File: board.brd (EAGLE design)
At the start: 85 parts, among them J1 AVR_SPI_PRG_6NS, U1 TPS2112A, U2 MAX1555, U3 USD-SOCKETNEW, U4 3.3V, U5 2.8V, U6 74HC595, Y1 8MHz, Y2 12.288MHz

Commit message: 0.1" shrink on y axis
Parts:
- moved JP2 14.9 mm to (41.6, 1.91)
- moved C7 12.8 mm to (64.1, 15.1)
- moved C13 2.54 mm to (21.0, 34.9)
- moved C9 2.54 mm to (19.1, 34.9)
- moved R15 2.54 mm to (41.9, 34.9)
- moved R9 2.54 mm to (38.7, 34.9)
- moved C16 2.54 mm to (23.8, 31.1)
- moved LED3 2.54 mm to (40.3, 16.2)
- moved LED6 2.54 mm to (40.3, 21.9)
- moved R11 2.54 mm to (23.8, 29.5)
- moved R13 2.54 mm to (23.8, 27.6)
- moved R23 2.54 mm to (44.5, 16.2)
- moved R26 2.54 mm to (44.5, 21.9)
- moved R6 2.54 mm to (22.2, 19.7)
- moved U1 2.54 mm to (8.26, 31.1)
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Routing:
- net SERIAL_TX: track 12.0 -> 22.1 mm
- net SERIAL_RX: track 10.7 -> 18.9 mm
- net VDD: track 243.3 -> 241.6 mm, vias 8 -> 9
- net ENCODER_A: track 39.5 -> 40.6 mm
- net ENCODER_B: track 34.5 -> 33.8 mm

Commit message: Moved SPI header to fit battery
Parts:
- moved J1 2.71 mm to (5.40, 5.08)
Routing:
- net VDD: track 241.6 -> 236.6 mm
- net RESET: track 15.4 -> 18.3 mm
- net MOSI: track 88.4 -> 86.2 mm
- net SCK: track 74.3 -> 76.3 mm, vias 2 -> 3
- net MISO: track 84.0 -> 82.1 mm
- net SERIAL_TX: track 22.1 -> 21.3 mm
- net SERIAL_RX: track 18.9 -> 18.3 mm
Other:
- board outline added: 50.8 x 33.5 mm

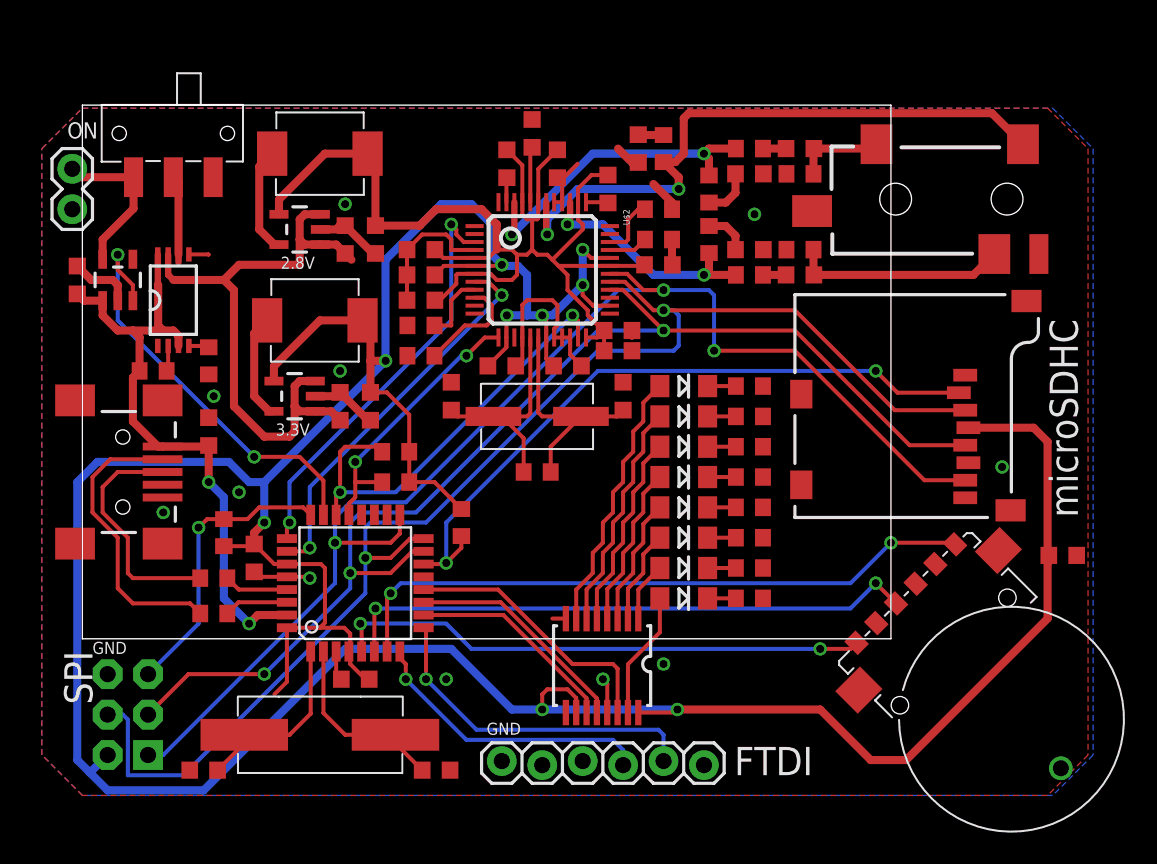
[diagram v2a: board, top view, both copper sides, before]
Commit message: Moved battery plug and SD capacitor
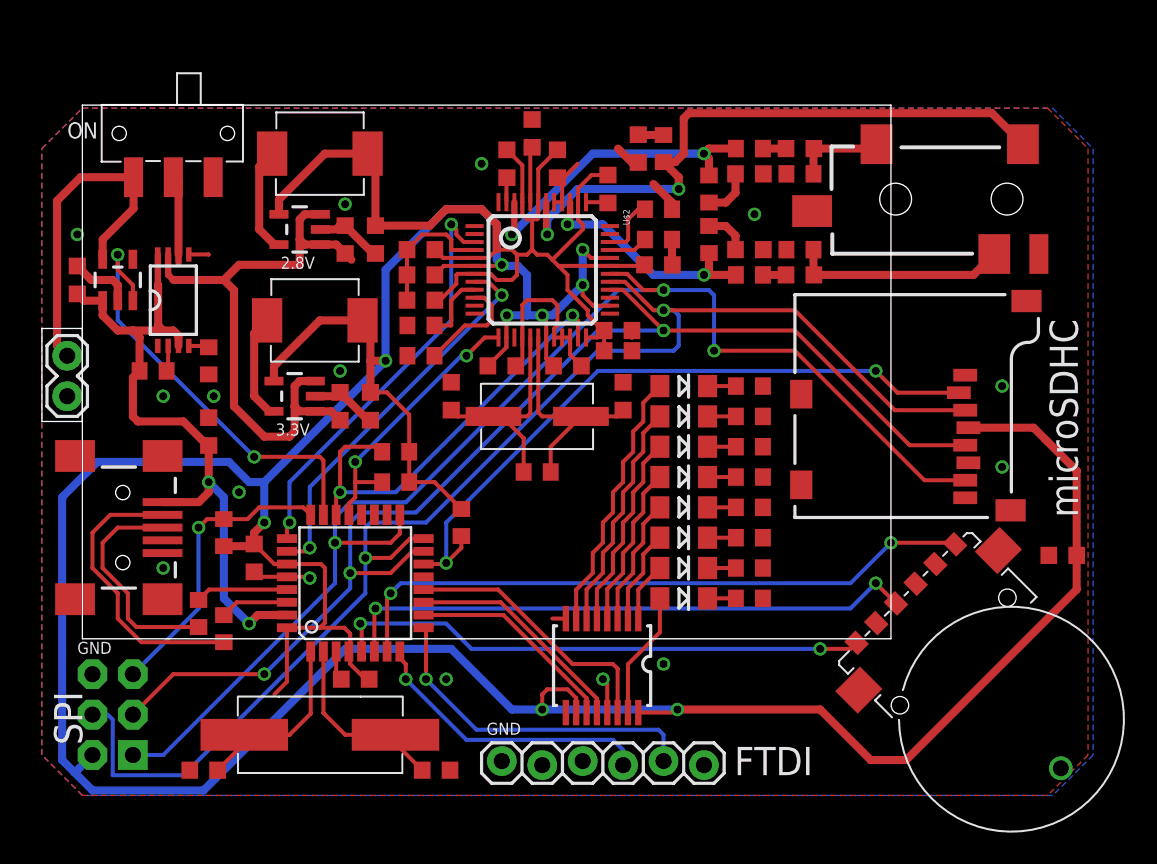
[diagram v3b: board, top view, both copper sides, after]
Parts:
- moved JP3 11.8 mm to (1.59, 27.6)
- moved JP1 3.49 mm to (5.08, 16.8)
- moved R2 2.42 mm to (9.84, 11.4), turned to 270 degrees
- moved R1 1.14 mm to (11.4, 10.5), turned to 270 degrees
- moved J1 0.95 mm to (4.45, 5.08)
- turned C7 to 180 degrees
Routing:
- net VBAT: track 10.0 -> 21.4 mm
- net VBUS: track 39.9 -> 43.5 mm
- net VDD: track 236.6 -> 238.5 mm
- net USB_D+: track 4.04 -> 5.82 mm
- net SCK: track 76.3 -> 77.3 mm
- net MISO: track 82.1 -> 83.1 mm
- net MOSI: track 86.2 -> 87.2 mm
- net CHG_B: track 26.7 -> 27.4 mm
- net N$6: track 14.9 -> 14.3 mm
- net GND: vias 11 -> 15
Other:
- board size 50.8 x 33.5 mm -> 53.3 x 33.5 mm

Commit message: Switched audio plug to 3-pin version and added OE connection
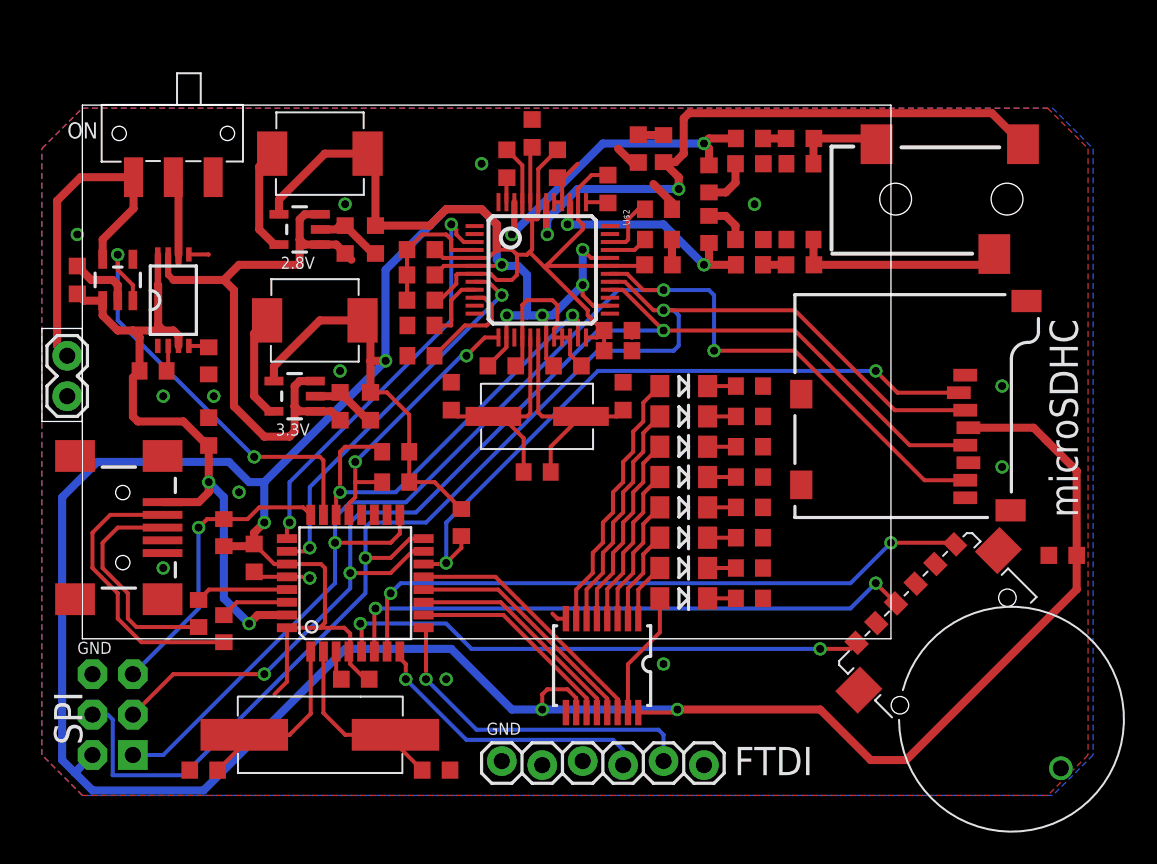
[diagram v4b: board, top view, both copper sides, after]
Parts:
- U7: device SparkFun-Connectors:AUDIO-JACK-3.5MM-SMD -> mkmp3:AUDIO-JACK-3.5MM-SMD
- moved R15 0.64 mm to (41.9, 35.6)
- moved C27 0.63 mm to (44.5, 34.9)
- moved C28 0.63 mm to (44.5, 39.7)
- moved C29 0.63 mm to (47.6, 41.3)
- moved C30 0.63 mm to (47.6, 33.3)
- moved R16 0.63 mm to (41.9, 38.7)
- moved R17 0.63 mm to (44.5, 41.3)
- moved R18 0.63 mm to (44.5, 33.3)
- moved R19 0.63 mm to (47.6, 34.9)
- moved R20 0.63 mm to (47.6, 39.7)
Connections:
- new net SHIFT_OE: U$1.12, U6.13
- net DS: now also U$1.13; no longer U$1.12
- net GND: no longer U6.13
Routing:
- net SHIFT_OE: track 0.00 -> 15.3 mm
- net GND: track 57.0 -> 54.9 mm, vias 15 -> 14
- net CVDD: track 72.3 -> 73.3 mm
- net DS: track 17.0 -> 16.2 mm

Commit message: Fixed rear silkscreen
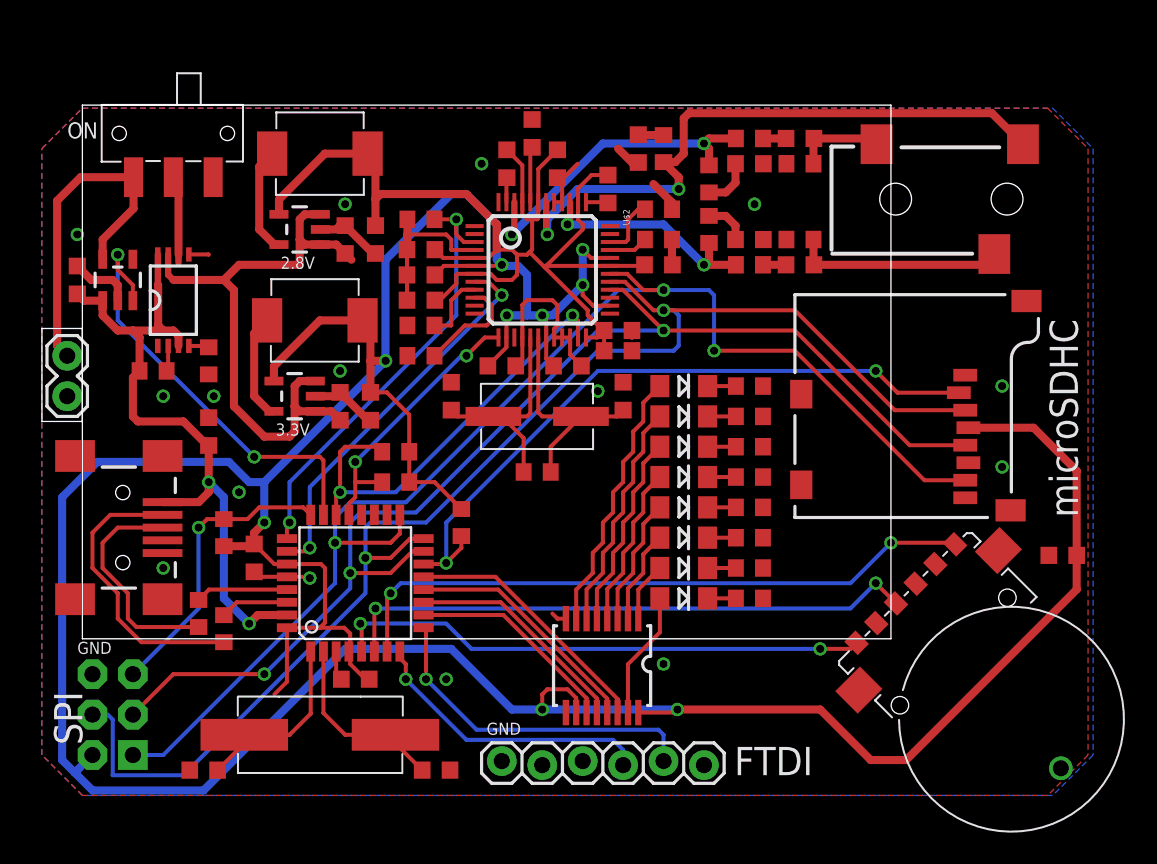
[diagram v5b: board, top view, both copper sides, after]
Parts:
- added R29: 100k, rcl:R0603W
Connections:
- net DS renamed SHIFT_DS
- net SHCP renamed SHIFT_SHCP
- net STCP renamed SHIFT_STCP
- net GND: now also R29.2
- net MP3_XRESET: now also R29.1
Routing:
- net MP3_XRESET: track 26.1 -> 28.1 mm
- net GND: track 54.9 -> 56.4 mm, vias 14 -> 15
- net VDD: track 238.5 -> 239.7 mm

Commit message: Capacitor value fixes and obsessive pcb trace cleanup
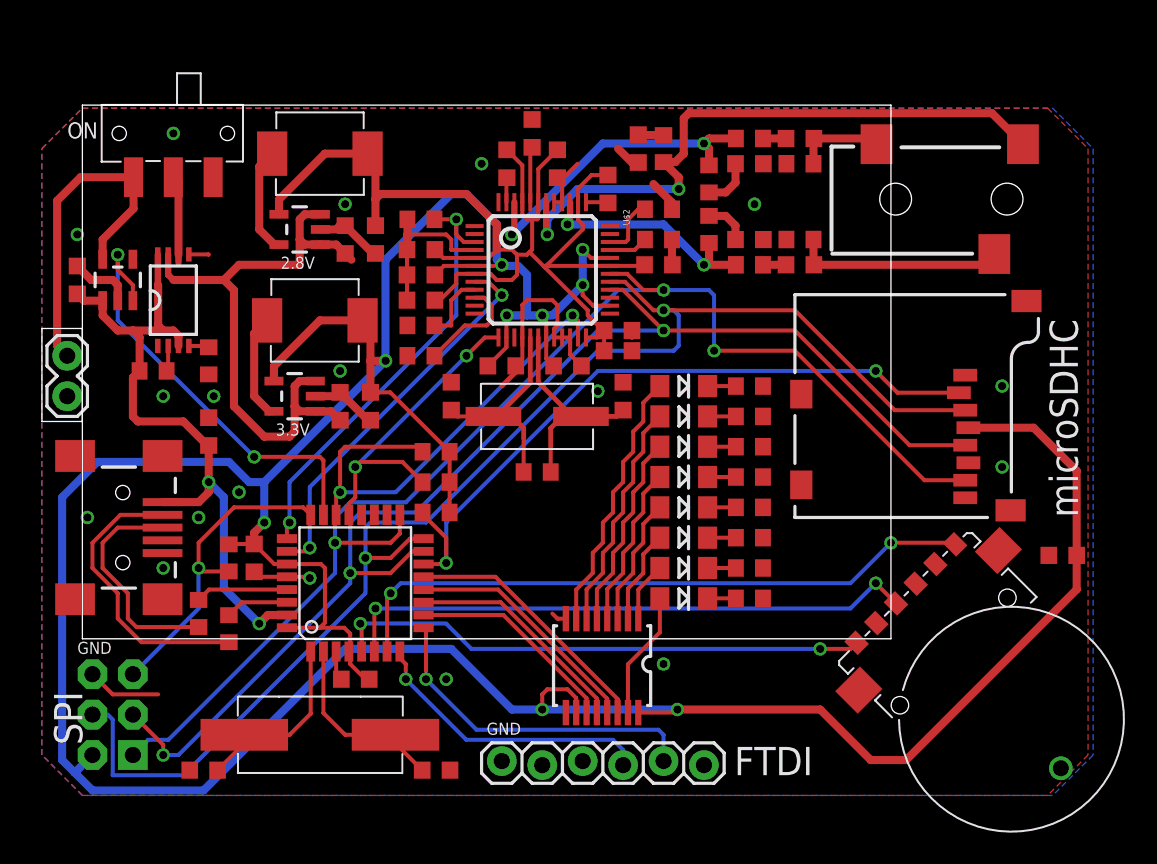
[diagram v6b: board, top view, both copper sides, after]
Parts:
- C10, C11: value 20p -> 33p
- C3, C4: value 18p -> 33p
- R1, R2, R8: device rcl:R0603 -> rcl:R0603W
- moved R6 2.54 mm to (24.8, 19.7)
- moved R7 2.54 mm to (24.8, 21.6)
- moved R8 1.71 mm to (24.8, 17.8), turned to 0 degrees
- moved R5 1.62 mm to (11.7, 14.9), turned to 90 degrees
- moved R1 0.32 mm to (11.7, 10.5)
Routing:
- net VDD: track 239.7 -> 233.9 mm
- net GND: track 56.4 -> 62.1 mm, vias 15 -> 18
- net MP3_XDCS: track 17.4 -> 20.4 mm
- net SCK: track 77.3 -> 79.9 mm
- net MP3_XCS: track 27.8 -> 30.3 mm
- net SD_CS: track 42.8 -> 44.5 mm
- net RESET: track 18.7 -> 20.1 mm
- net N$7: track 14.6 -> 13.4 mm
- net N$8: track 14.0 -> 13.3 mm

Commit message: More board cleanup
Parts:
- C25: value 1u -> 0.1u
- moved JP3 0.64 mm to (2.22, 27.6)
- moved R13 0.32 mm to (23.8, 27.9)
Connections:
- net SD_CD: now also U$1.18
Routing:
- net SD_CD: track 0.00 -> 34.8 mm, vias 0 -> 2
- net SD_CS: track 44.5 -> 43.2 mm
- net CVDD: track 73.4 -> 72.1 mm
- net SCK: track 79.9 -> 80.9 mm
- net MISO: track 82.7 -> 83.6 mm
- net VDD: track 233.9 -> 233.3 mm
- net GND: vias 18 -> 24
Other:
- board size 53.3 x 33.5 mm -> 67.3 x 44.4 mm
- board text added: "ICSP"
- board text added: "MJK 09/13"
- board text added: "mattkeeter.com"
- board text removed: "MJK 09/13 mattkeeter.com"
- board text removed: "SPI"
